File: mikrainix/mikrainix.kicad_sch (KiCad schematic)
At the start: 0 parts

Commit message: update SPLink schematic
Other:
- removed sheet U_CAMERA_MPU
- removed sheet U_IO_MPU
- removed sheet U_LPDDR4_MPU
- removed sheet U_PMIC_MPU
- removed sheet U_PWR_MPU
- removed sheet U_SDMMC_MPU
- removed sheet U_USB_MPU

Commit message: add USB WiFi and update MPU RV1106G3 schematics
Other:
- added sheet U_MPU-Clock-Reset-Boot-Gpio (MPU-Clock-Reset-Boot-Gpio.kicad_sch)
- added sheet U_MPU-PowerSupply (MPU-PowerSupply.kicad_sch)
- added sheet U_MPU-USB-Wifi (MPU-USB-Wifi.kicad_sch)
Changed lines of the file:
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@@
 	(paper "A4")
 	(sheet
-		(at 44.45 50.8)
-		(size 25.4 12.7)
+		(at 101.6 76.2)
+		(size 50.8 12.7)
+		(exclude_from_sim no)
+		(in_bom yes)
+		(on_board yes)
+		(dnp no)
+		(fields_autoplaced yes)
+		(stroke
+			(width 0.1524)
+			(type solid)
+		)
+		(fill
+			(color 0 0 0 0)
+		)
+		(property "Sheetname" "U_MPU-USB-Wifi"
+			(at 101.6 75.4884 0)
+			(show_name no)
+			(do_not_autoplace no)
+			(effects
+				(font
+					(size 1.27 1.27)
+				)
+				(justify left bottom)
+			)
+		)
+		(property "Sheetfile" "MPU-USB-Wifi.kicad_sch"
+			(at 101.6 89.4846 0)
+			(show_name no)
+			(do_not_autoplace no)
+			(effects
+				(font
+					(size 1.27 1.27)
+				)
+				(justify left top)
+			)
+		)
+		(instances
+			(project "mikrainix"
+				(path "/19082ed6-8f17-4d62-ab42-418ea03b55ea"
+					(page "5")
+				)
+			)
+		)
+	)
+	(sheet
+		(at 38.1 50.8)
+		(size 50.8 12.7)
 		(exclude_from_sim no)
 		(in_bom yes)
@@
 		)
 		(property "Sheetname" "U_SPLink"
-			(at 44.45 50.0884 0)
+			(at 38.1 50.0884 0)
 			(show_name no)
 			(do_not_autoplace no)
@@
 		)
 		(property "Sheetfile" "SPLink.kicad_sch"
-			(at 44.45 64.0846 0)
+			(at 38.1 64.0846 0)
 			(show_name no)
 			(do_not_autoplace no)
@@
 				)
 			)
+		)
+	)
+	(sheet
+		(at 101.6 50.8)
+		(size 50.8 12.7)
+		(exclude_from_sim no)
+		(in_bom yes)
+		(on_board yes)
+		(dnp no)
+		(fields_autoplaced yes)
+		(stroke
+			(width 0.1524)
+			(type solid)
+		)
+		(fill
+			(color 0 0 0 0)
+		)
+		(property "Sheetname" "U_MPU-PowerSupply"
+			(at 101.6 50.0884 0)
+			(show_name no)
+			(do_not_autoplace no)
+			(effects
+				(font
+					(size 1.27 1.27)
+				)
+				(justify left bottom)
+			)
+		)
+		(property "Sheetfile" "MPU-PowerSupply.kicad_sch"
+			(at 101.6 64.0846 0)
+			(show_name no)
+			(do_not_autoplace no)
+			(effects
+				(font
+					(size 1.27 1.27)
+				)
+				(justify left top)
+			)
+		)
+		(instances
+			(project "mikrainix"
+				(path "/19082ed6-8f17-4d62-ab42-418ea03b55ea"
+					(page "3")
+				)
+			)
+		)
+	)
+	(sheet
+		(at 38.1 76.2)
+		(size 50.8 12.7)
+		(exclude_from_sim no)
+		(in_bom yes)
+		(on_board yes)
+		(dnp no)
+		(fields_autoplaced yes)
+		(stroke
+			(width 0.1524)
+			(type solid)
+		)
+		(fill
+			(color 0 0 0 0)
+		)
+		(property "Sheetname" "U_MPU-Clock-Reset-Boot-Gpio"
+			(at 38.1 75.4884 0)
+			(show_name no)
+			(do_not_autoplace no)
+			(effects
+				(font
+					(size 1.27 1.27)
+				)
+				(justify left bottom)
+			)
+		)
+		(property "Sheetfile" "MPU-Clock-Reset-Boot-Gpio.kicad_sch"
+			(at 38.1 89.4846 0)
+			(show_name no)
+			(do_not_autoplace no)
+			(effects
+				(font
+					(size 1.27 1.27)
+				)
+				(justify left top)
+			)
+		)
+		(instances
+			(project "mikrainix"
+				(path "/19082ed6-8f17-4d62-ab42-418ea03b55ea"
+					(page "4")
+				)
+			)

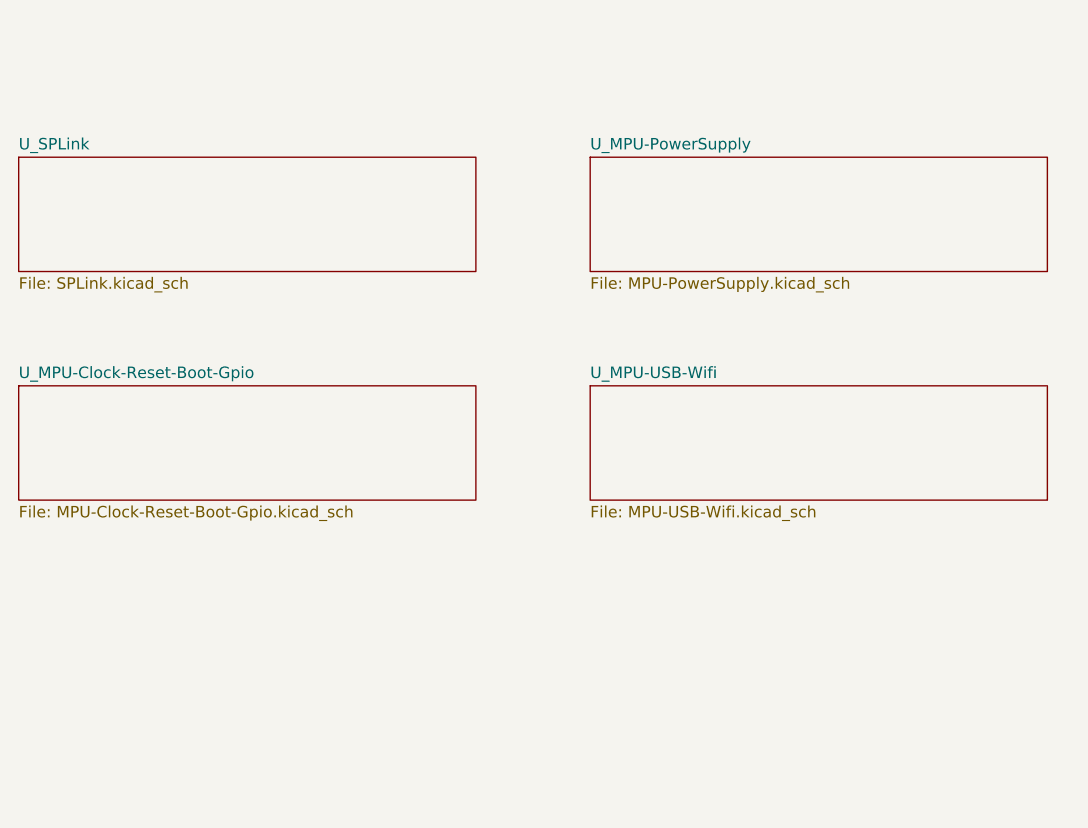
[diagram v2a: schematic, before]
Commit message: add MIS5001 camera and Ethernet, replace ESP32-C6-MINI > ESP32-MINI-1
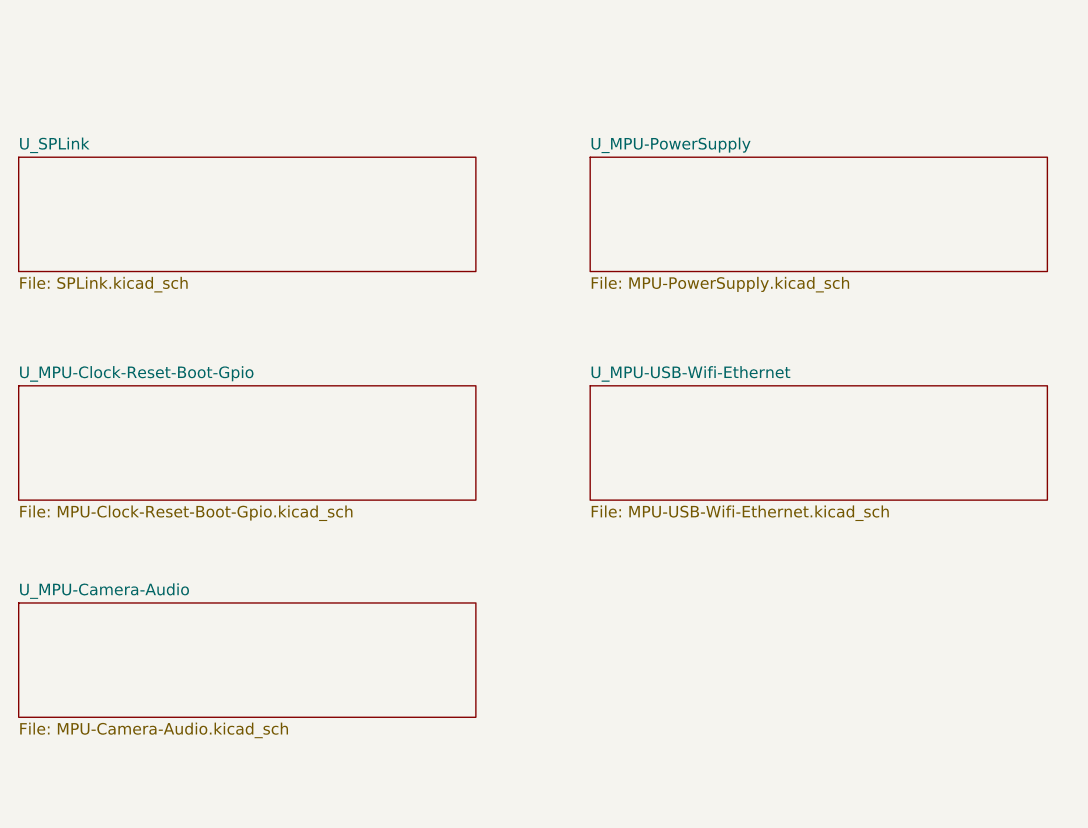
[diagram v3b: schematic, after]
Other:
- sheet U_MPU-USB-Wifi renamed U_MPU-USB-Wifi-Ethernet
- added sheet U_MPU-Camera-Audio (MPU-Camera-Audio.kicad_sch)
- sheet U_MPU-USB-Wifi-Ethernet: file MPU-USB-Wifi.kicad_sch -> MPU-USB-Wifi-Ethernet.kicad_sch
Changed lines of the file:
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@@
 			(color 0 0 0 0)
 		)
-		(property "Sheetname" "U_MPU-USB-Wifi"
+		(property "Sheetname" "U_MPU-USB-Wifi-Ethernet"
 			(at 101.6 75.4884 0)
 			(show_name no)
@@
 			)
 		)
-		(property "Sheetfile" "MPU-USB-Wifi.kicad_sch"
+		(property "Sheetfile" "MPU-USB-Wifi-Ethernet.kicad_sch"
 			(at 101.6 89.4846 0)
 			(show_name no)
@@
 				)
 			)
+		)
+	)
+	(sheet
+		(at 38.1 100.33)
+		(size 50.8 12.7)
+		(exclude_from_sim no)
+		(in_bom yes)
+		(on_board yes)
+		(dnp no)
+		(fields_autoplaced yes)
+		(stroke
+			(width 0.1524)
+			(type solid)
+		)
+		(fill
+			(color 0 0 0 0)
+		)
+		(property "Sheetname" "U_MPU-Camera-Audio"
+			(at 38.1 99.6184 0)
+			(show_name no)
+			(do_not_autoplace no)
+			(effects
+				(font
+					(size 1.27 1.27)
+				)
+				(justify left bottom)
+			)
+		)
+		(property "Sheetfile" "MPU-Camera-Audio.kicad_sch"
+			(at 38.1 113.6146 0)
+			(show_name no)
+			(do_not_autoplace no)
+			(effects
+				(font
+					(size 1.27 1.27)
+				)
+				(justify left top)
+			)
+		)
+		(instances
+			(project "mikrainix"
+				(path "/19082ed6-8f17-4d62-ab42-418ea03b55ea"
+					(page "6")
+				)
+			)

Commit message: add microSD and resolve ERC issues
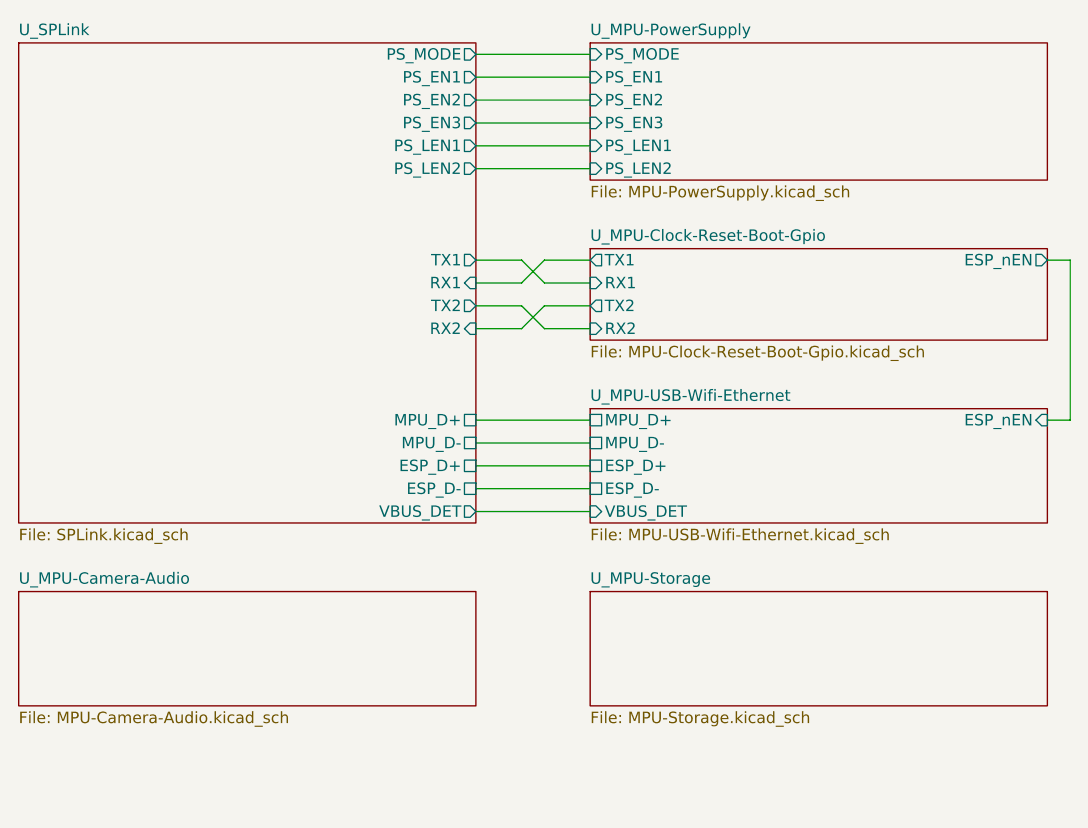
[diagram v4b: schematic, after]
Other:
- added sheet U_MPU-Storage (MPU-Storage.kicad_sch)
- sheet U_MPU-Clock-Reset-Boot-Gpio ports: added ESP_nEN, RX1, RX2, TX1, TX2; removed none
- sheet U_MPU-PowerSupply ports: added PS_EN1, PS_EN2, PS_EN3, PS_LEN1, PS_LEN2, PS_MODE; removed none
- sheet U_MPU-USB-Wifi-Ethernet ports: added ESP_D+, ESP_D-, ESP_nEN, MPU_D+, MPU_D-, VBUS_DET; removed none
- sheet U_SPLink ports: added ESP_D+, ESP_D-, MPU_D+, MPU_D-, PS_EN1, PS_EN2, PS_EN3, PS_LEN1, PS_LEN2, PS_MODE, RX1, RX2, TX1, TX2, VBUS_DET; removed none
- title: (none) -> Mikrainix
